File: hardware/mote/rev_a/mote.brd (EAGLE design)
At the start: 160 x 100 mm, 139 parts, among them J1 TC2030-JLINK-L, J2 TC2030-JLINK-NL, Q1 CSD22206W, Q10 CSD22206W, Q11 CSD22206W, Q2 CSD22206W, Q6 CSD22206W, Q7 CSD22206W, Q8 CSD22206W, Q9 CSD22206W, U1 NRF52840, U10 MS5637-02BA03, U11 ADP5091, U12 NRF51822QF, U3 MAX17222, U4 AMN41121, U5 SI7021-A20-GM1, U6 ISL29125, U7 MAX44009, U8 LIS2DW12, U9 AB1815-T3, X1 7V-32.000MAHV-T, X2 ABS05-32.768KHZ-9-T, X3 ABS07-32.768KHZ-7-T, X5 16MHz, X6 ABS05-32.768KHZ-9-T

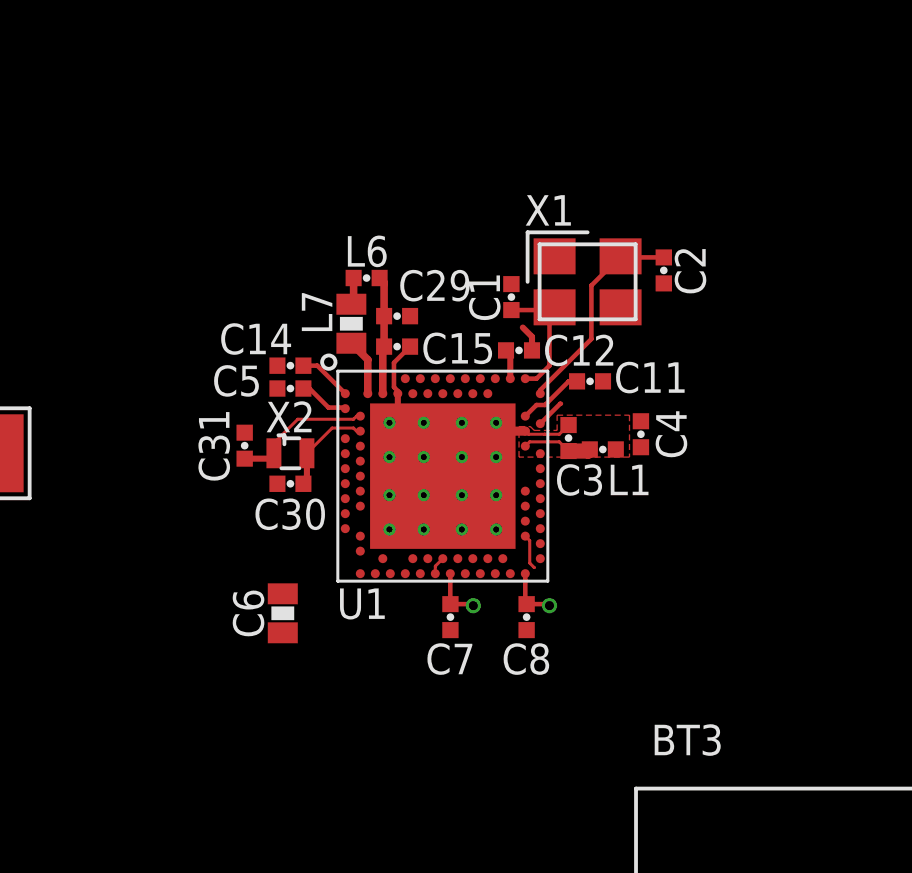
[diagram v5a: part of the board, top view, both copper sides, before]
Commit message: route signals out of mcu
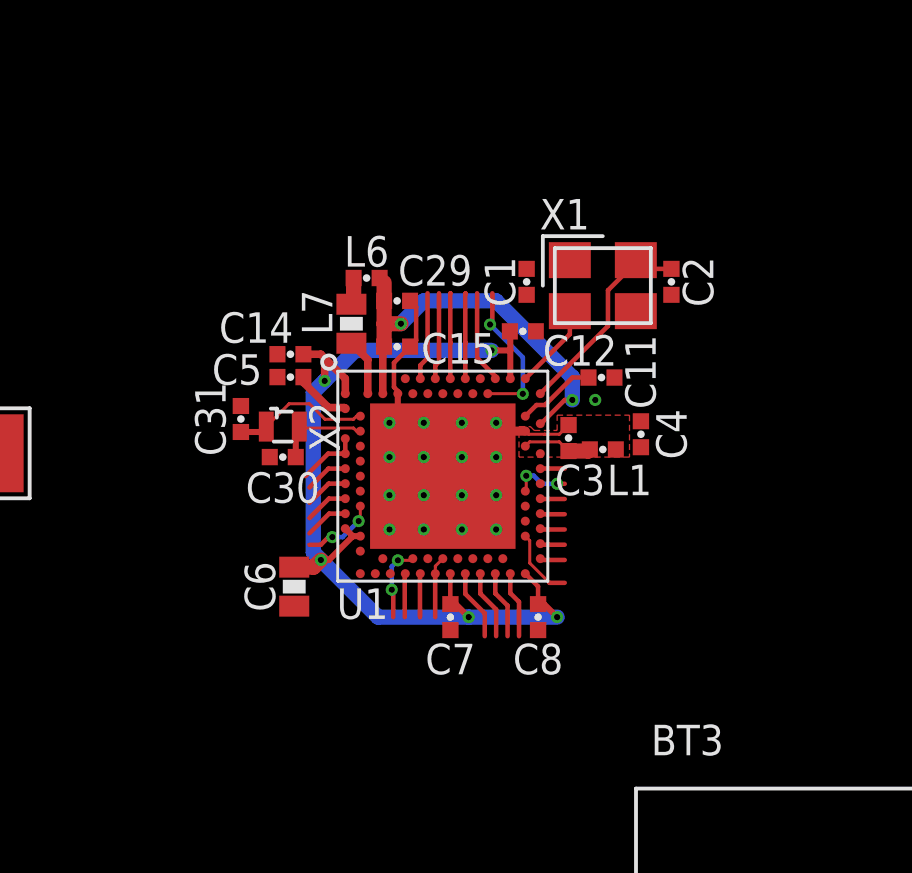
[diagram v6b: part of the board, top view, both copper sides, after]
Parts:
- moved C6 0.97 mm to (44.6, 46.1)
- moved X2 0.92 mm to (44.2, 51.4)
- moved C30 0.92 mm to (44.2, 50.4)
- moved C31 0.90 mm to (42.8, 51.7)
- moved C1 0.72 mm to (52.3, 56.3)
- moved C12 0.65 mm to (52.2, 54.6)
- moved X1 0.52 mm to (54.9, 56.1)
- moved C29 0.51 mm to (48.0, 55.6)
- moved C2 0.46 mm to (57.1, 56.3)
- moved C11 0.40 mm to (54.8, 53.1)
- moved C14 0.38 mm to (44.5, 53.8)
- moved C5 0.38 mm to (44.5, 53.1)
- moved C8 0.38 mm to (52.7, 45.1)
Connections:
- removed net CLKOUT: U9.8
- new net !RTC_IRQ3: U1.P23, U9.8
- net !CLR_EN: now also U1.T2; no longer U1.AD16
- net !I2C_EN: now also U1.B19
- net !RTC_IRQ1: now also U1.AC9
- net !RTC_IRQ2: now also U1.AD16
- net ACC_CS: now also U1.AD8; no longer U1.AD10
- net RTC_CS: now also U1.AD10; no longer U1.AD8
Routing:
- net N$39: track 6.40 -> 32.9 mm, vias 2 -> 5
- net N$3: track 4.90 -> 13.7 mm, vias 0 -> 2
- net !I2C_EN: track 0.00 -> 5.01 mm, vias 0 -> 2
- net !PIR_EN: track 0.00 -> 3.10 mm
- net VBAT: track 0.00 -> 2.95 mm
- net VSEC: track 0.00 -> 2.90 mm
- net !LT_EN: track 0.00 -> 2.87 mm
- net !ACC_EN: track 0.00 -> 2.85 mm
- net !RTC_IRQ1: track 0.00 -> 2.52 mm, vias 0 -> 2
- net !CLR_EN: track 0.00 -> 2.49 mm, vias 0 -> 2
- net !RTC_IRQ2: track 0.00 -> 2.35 mm
- net SCK: track 0.00 -> 2.30 mm
- net MOSI: track 0.00 -> 2.25 mm
- net MISO: track 0.00 -> 2.20 mm
- net SW: track 19.2 -> 21.3 mm
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
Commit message: finished most of front end
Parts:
- moved C27 665.8 mm to (69.5, 83.6)
- moved C28 656.6 mm to (48.9, 85.0)
- moved R22 642.9 mm to (64.4, 77.9), turned to 270 degrees
- moved L2 642.6 mm to (70.6, 78.4), turned to 180 degrees
- moved R20 641.9 mm to (65.5, 87.9), turned to 270 degrees
- moved R18 640.8 mm to (58.0, 96.5)
- moved R21 639.0 mm to (63.4, 77.9), turned to 90 degrees
- moved C26 637.7 mm to (63.6, 80.3), turned to 270 degrees
- moved R19 634.0 mm to (61.0, 84.8)
- moved R16 627.5 mm to (63.1, 88.8), turned to 180 degrees
- moved R17 623.3 mm to (60.5, 81.4), turned to 270 degrees
- moved R15 616.3 mm to (61.5, 81.4), turned to 90 degrees
- moved R6 614.8 mm to (61.0, 83.8), turned to 180 degrees
- moved R5 613.1 mm to (61.0, 85.9), turned to 180 degrees
- moved R1 607.9 mm to (63.1, 87.4)
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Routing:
- net VBAT: track 2.95 -> 114.3 mm
- net N$10: track 0.00 -> 15.0 mm
- net N$38: track 0.00 -> 11.4 mm
- net N$45: track 0.00 -> 10.0 mm
- net VSEC: track 2.90 -> 9.92 mm
- net N$32: track 0.00 -> 5.32 mm
- net VSW: track 7.79 -> 12.7 mm
- net GND: track 21.0 -> 25.5 mm, vias 37 -> 50
- net N$1: track 0.00 -> 4.42 mm
- net N$13: track 0.00 -> 4.21 mm
- net N$11: track 0.00 -> 3.20 mm
- net N$17: track 0.00 -> 3.01 mm
- net N$16: track 0.00 -> 2.44 mm
- net N$47: track 0.00 -> 2.05 mm
- net N$30: track 0.00 -> 1.79 mm
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
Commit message: Rearrange a bit
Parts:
- moved TP23 460.5 mm to (27.7, 64.0)
- moved JP6 448.9 mm to (26.3, 60.2)
- moved TP22 444.8 mm to (24.0, 64.0)
- moved U8 223.9 mm to (20.2, 89.9)
- moved C25 219.1 mm to (23.2, 60.7), turned to 90 degrees
- moved C22 216.3 mm to (22.0, 61.2)
- moved X3 210.4 mm to (18.7, 62.5)
- moved C24 210.3 mm to (21.6, 62.7), turned to 90 degrees
- moved C17 209.6 mm to (7.24, 60.2)
- moved C23 208.4 mm to (15.7, 62.5), turned to 90 degrees
- moved C9 205.3 mm to (8.00, 57.1)
- moved U9 204.6 mm to (19.2, 58.8)
- moved TP11 119.5 mm to (42.3, 7.37)
- moved B2 114.0 mm to (68.5, 54.7)
- moved C46 114.0 mm to (63.8, 55.9)
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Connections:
- removed net N$43: JP6.2, TP23.TESTPOINT
- net VBAT: now also JP6.2, TP23.TESTPOINT
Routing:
- net VBATT: track 15.9 -> 0.00 mm
- net N$42: track 0.00 -> 10.8 mm
- net VBAT: track 114.3 -> 121.7 mm
- net N$27: track 0.00 -> 4.89 mm
- net N$26: track 0.00 -> 4.58 mm
- net N$25: track 0.00 -> 2.97 mm
- net !RTC_IRQ3: track 1.92 -> 2.81 mm
- net RTC_CS: track 1.45 -> 2.27 mm
- net SCK: track 2.30 -> 3.06 mm
- net MISO: track 2.20 -> 2.96 mm
- net MOSI: track 2.25 -> 2.94 mm
- net !RTC_IRQ1: track 2.52 -> 3.20 mm
